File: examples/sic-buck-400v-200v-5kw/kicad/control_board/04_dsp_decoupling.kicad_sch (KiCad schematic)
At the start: 33 parts

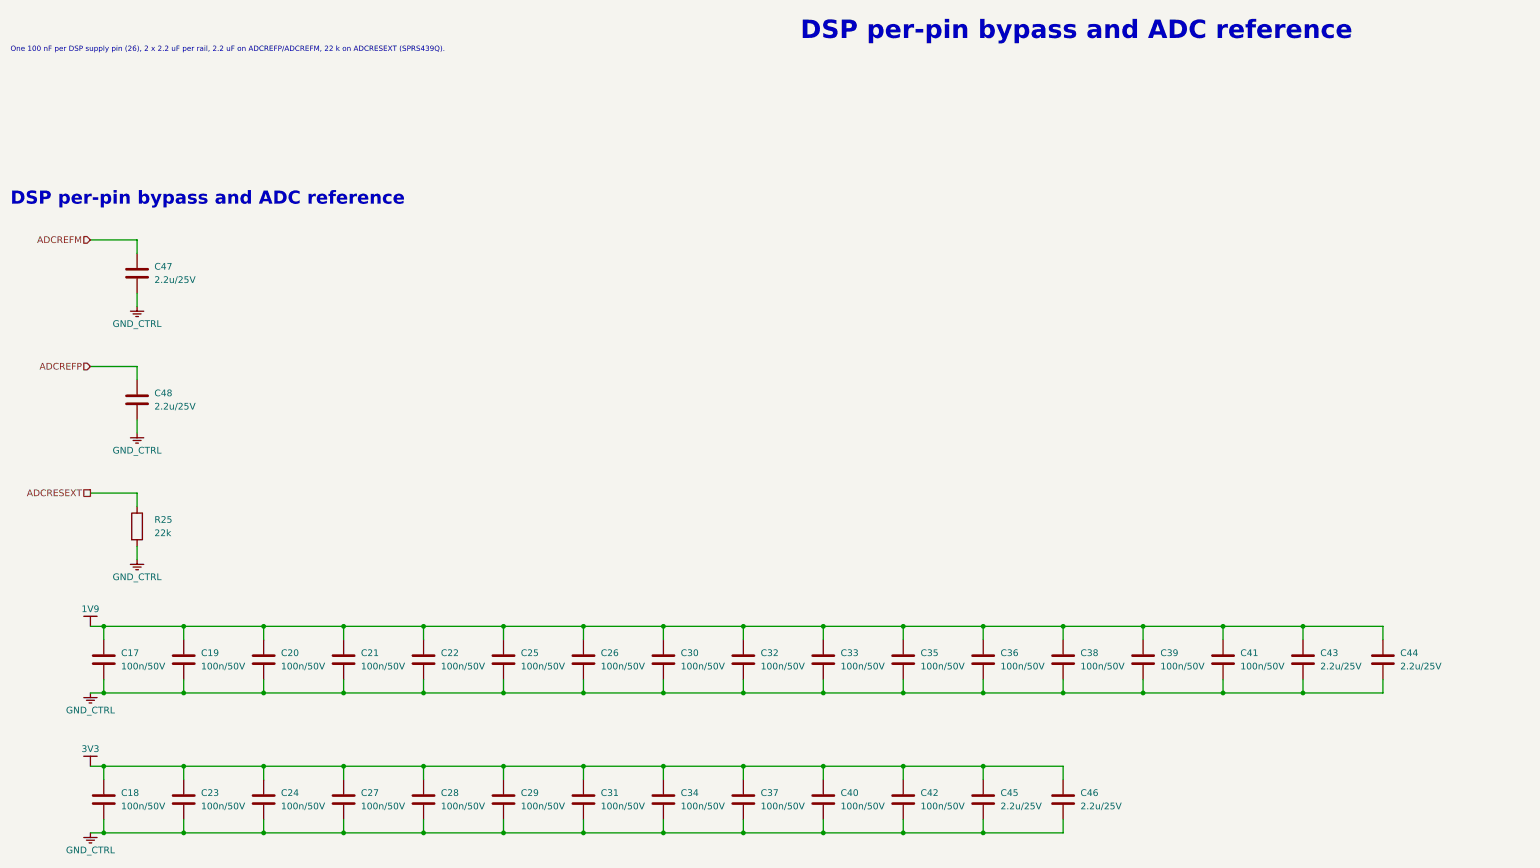
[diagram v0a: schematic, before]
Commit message: Correct sensing circuits and add verified V2.2 local bypasses
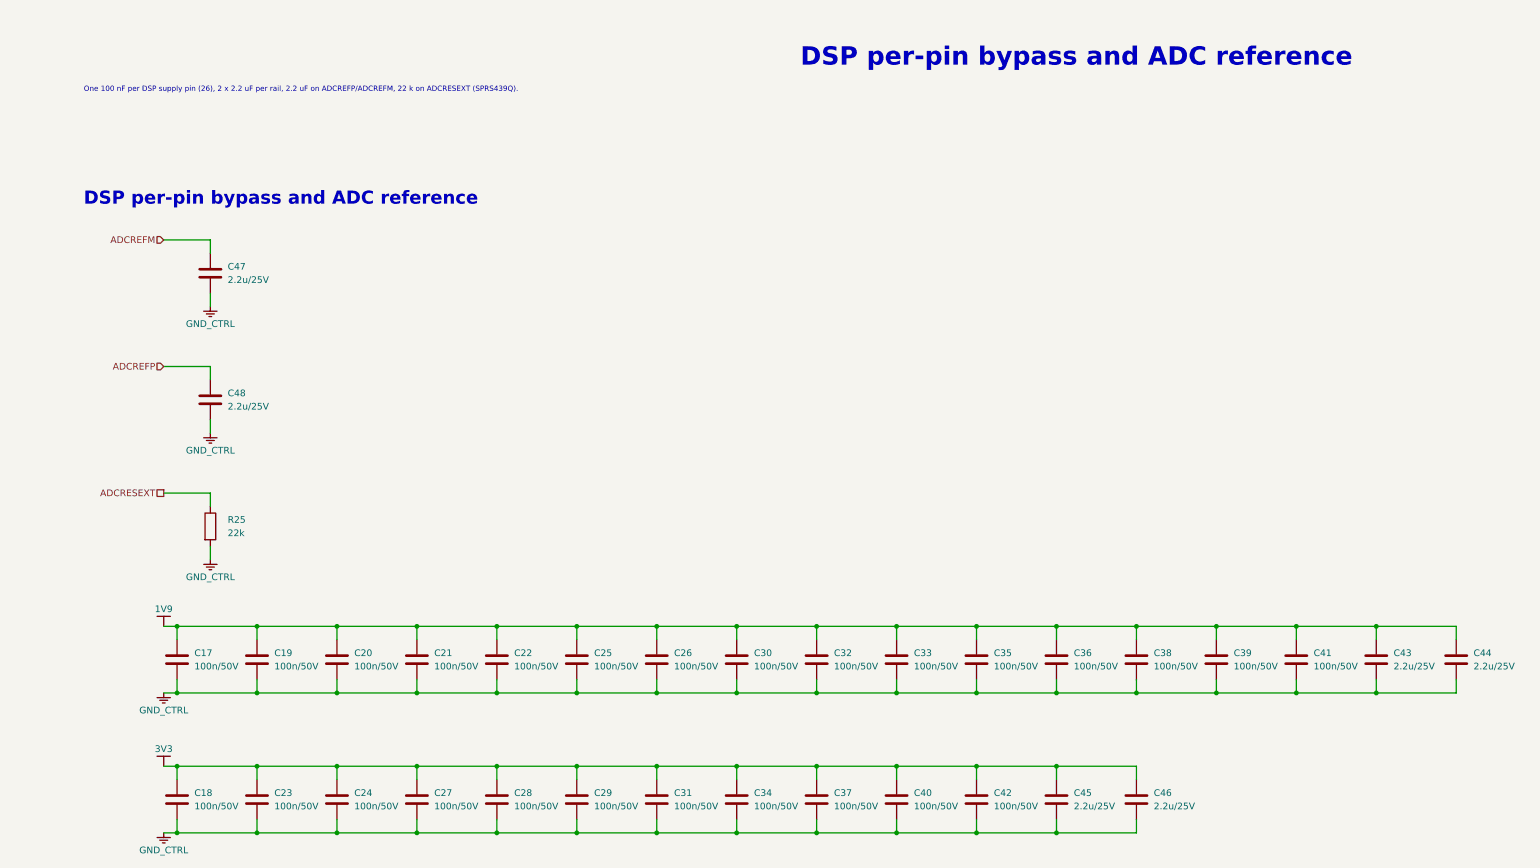
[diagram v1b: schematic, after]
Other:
- moved on the sheet: C17, C18, C19, C20, C21, C22, C23, C24, C25, C26, C27, C28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
